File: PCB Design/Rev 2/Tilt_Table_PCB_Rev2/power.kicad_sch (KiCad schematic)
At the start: 52 parts, among them J1 2171750001, J12 BUCK_EN, J2 7x1 RECP, J3 PD_Output, Q1 DMP3098LSD-13, Q3 2N7002, U1 TPS54531DDA, U2 CYPD3177-24LQ

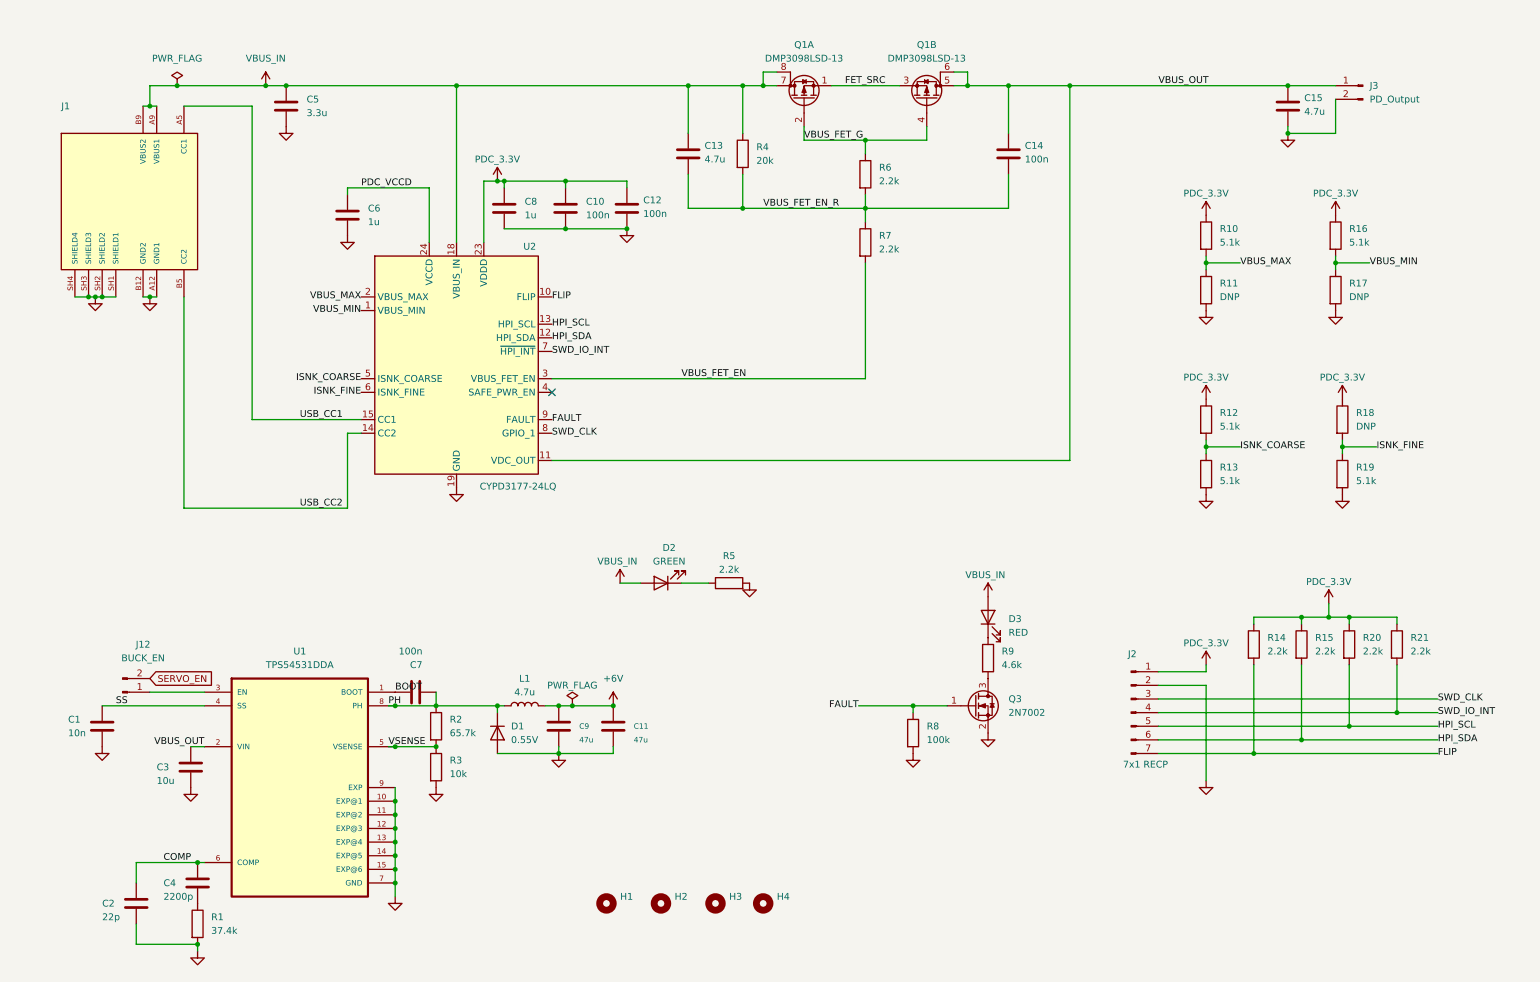
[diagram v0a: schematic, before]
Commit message: Rev 2 schematic updated
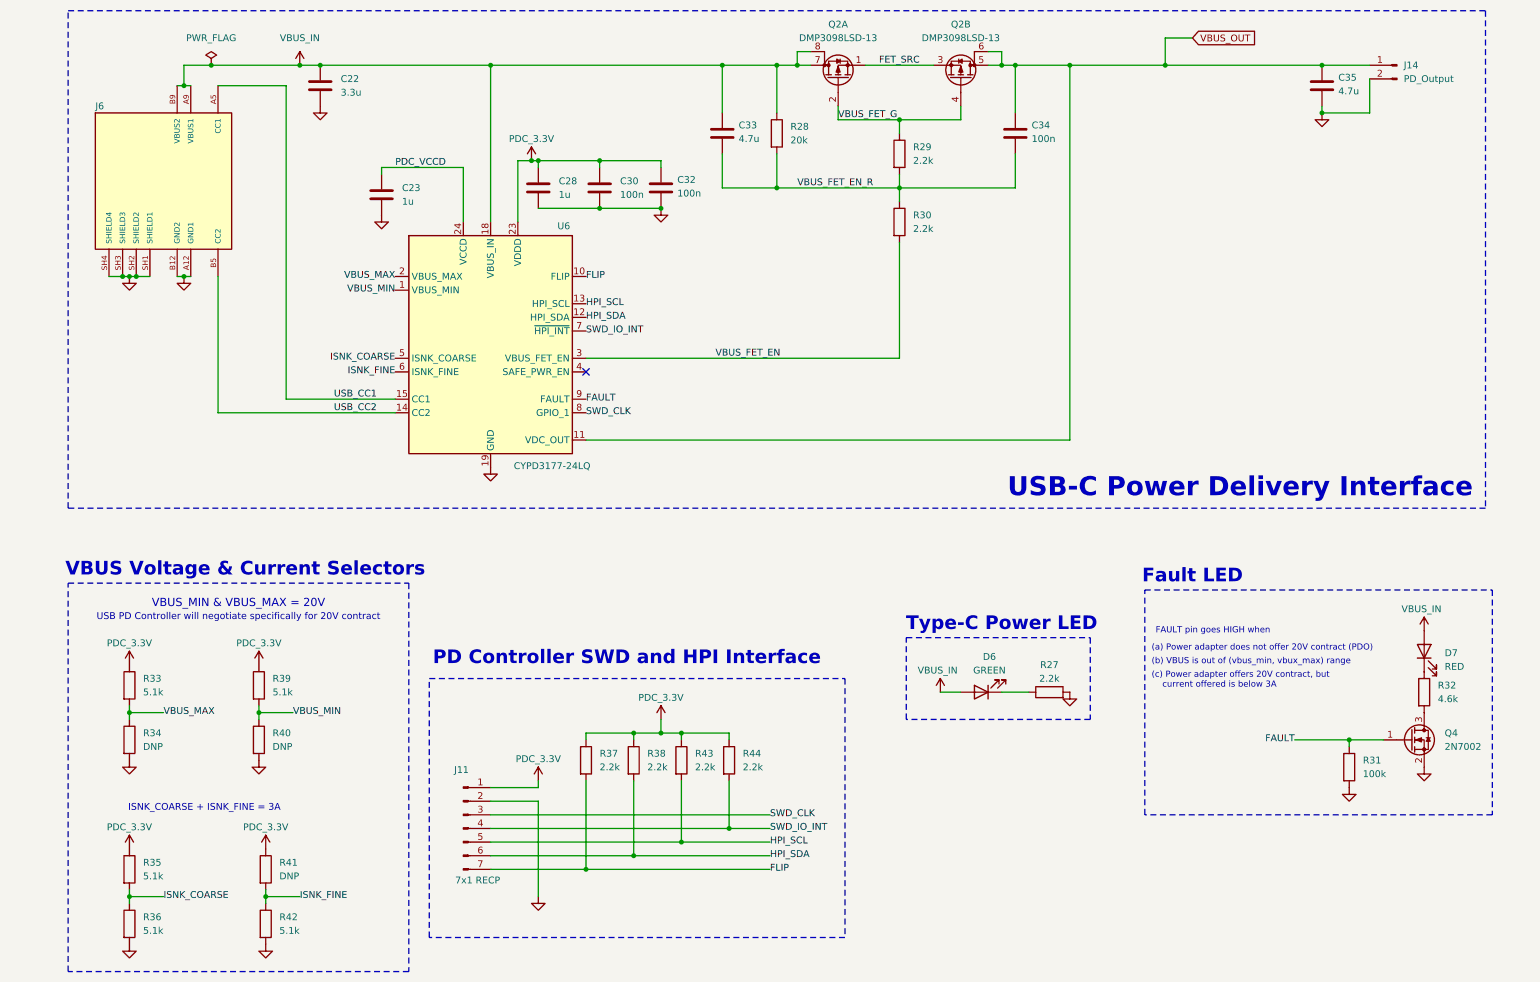
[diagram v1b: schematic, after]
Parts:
- removed C1: 10n, Capacitor_SMD:C_0603_1608Metric, symbol Device:C
- removed C11, C9: 47u, Capacitor_SMD:C_0805_2012Metric, symbol Device:C
- removed C2: 22p, Capacitor_SMD:C_0603_1608Metric, symbol Device:C
- removed C3: 10u, Capacitor_SMD:C_0805_2012Metric, symbol Device:C
- removed C4: 2200p, Capacitor_SMD:C_0603_1608Metric, symbol Device:C
- removed C7: 100n, Capacitor_SMD:C_0603_1608Metric, symbol Device:C
- removed D1: 0.55V, footprints:DIOM7959X262N, symbol Device:D
- removed H1, H2, H3, H4: MountingHole, MountingHole:MountingHole_3.2mm_M3, symbol Mechanical:MountingHole
- removed J12: BUCK_EN, Connector_PinHeader_2.54mm:PinHeader_1x02_P2.54mm_Vertical, symbol Connector:Conn_01x02_Pin
- removed L1: 4.7u, footprints:IND_SRR1240-4R7M, symbol Device:L
- removed R1: 37.4k, Resistor_SMD:R_0603_1608Metric, symbol Device:R
- removed R2: 65.7k, Resistor_SMD:R_0603_1608Metric, symbol Device:R
- removed R3: 10k, Resistor_SMD:R_0603_1608Metric, symbol Device:R
- removed U1: TPS54531DDA, footprints:VREG_LM5017MR_NOPB, symbol TPS54531DDA:TPS54531DDA
- renumbered C5 to C22, C6 to C23, C8 to C28, C10 to C30, C12 to C32, C13 to C33, C14 to C34, C15 to C35, D2 to D6, D3 to D7, J2 to J11, J3 to J14, J1 to J6, Q1 to Q2, Q3 to Q4, R5 to R27, R4 to R28, R6 to R29, R7 to R30, R8 to R31, R9 to R32, R10 to R33, R11 to R34, R12 to R35, R13 to R36, R14 to R37, R15 to R38, R16 to R39, R17 to R40, R18 to R41, R19 to R42, R20 to R43, R21 to R44, U2 to U6
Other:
- note added: "(a) Power adapter does not offer 20V contract (PDO)"
- note added: "(b) VBUS is out of (vbus_min, vbux_max) range"
- note added: "(c) Power adapter offers 20V contract, but current offered is below 3A"
- note added: "FAULT pin goes HIGH when"
- note added: "Fault LED"
- note added: "ISNK_COARSE + ISNK_FINE = 3A"
- note added: "PD Controller SWD and HPI Interface"
- note added: "Type-C Power LED"
- note added: "USB PD Controller will negotiate specifically for 20V contract"
- note added: "USB-C Power Delivery Interface"
- note added: "VBUS Voltage & Current Selectors"
- note added: "VBUS_MIN & VBUS_MAX = 20V"
- moved on the sheet: C22, C23, C28, C30, C32, C33, C34, C35, D6, D7, J11, J14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

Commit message: PCB Rev 2 Update
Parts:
- renumbered C22 to C1, C23 to C2, C28 to C3, C30 to C4, C32 to C5, C33 to C6, C34 to C7, C35 to C8, D6 to D1, D7 to D2, J6 to J1, J11 to J2, J14 to J3, Q2 to Q1, Q4 to Q2, R33 to R1, R38 to R10, R43 to R11, R44 to R12, R28 to R13, R29 to R14, R30 to R15, R27 to R16, R31 to R17, R32 to R18, R34 to R2, R35 to R3, R36 to R4, R39 to R5, R40 to R6, R41 to R7, R42 to R8, R37 to R9, U6 to U1
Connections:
- net FLIP: now also J2.5 (Pin_5), R11.2; no longer J2.7 (Pin_7), R9.2
- net GND: now also D1.1 (K); no longer R16.2
- net HPI_SCL: now also J2.7 (Pin_7), R9.2; no longer J2.5 (Pin_5), R11.2
- net SWD_CLK: now also J2.4 (Pin_4); no longer J2.3 (Pin_3)
- net SWD_IO_INT: now also J2.3 (Pin_3); no longer J2.4 (Pin_4)
- net VBUS_IN: now also Q1.5 (D), Q1.6 (D), R16.1; no longer D1.2 (A), Q1.7 (D), Q1.8 (D)
- net VBUS_OUT: now also Q1.7 (D), Q1.8 (D); no longer Q1.5 (D), Q1.6 (D)
- new net: D1.2 (A), R16.2
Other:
- company: (none) -> Made by Jasper Tan
- title: (none) -> Tilt Plate Board
- moved on the sheet: C1, C2, C3, C4, C5, C6, C7, C8, D1, J1, J3, Q1A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

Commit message: PCB Rev 2 Layout Complete - Prior to PCB Order
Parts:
- R18: value 4.6k -> 1k
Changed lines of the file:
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@@
 			)
 		)
-		(property "Value" "4.6k"
+		(property "Value" "1k"
 			(at 271.78 143.5099 0)
 			(effects
